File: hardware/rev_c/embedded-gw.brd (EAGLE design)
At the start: 38.5 x 66 mm, 57 parts, among them J1 DM3BT-DSF-PEJS, J2 TC2030-JLINK-NL, J3 USB-A-MALE-PLUG, Q1 QS5K2TR, U1 AP7362A-33SP-13, U2 BT840X, U3 CP2102N-20, U4 ESDR0502N, U5 ESP32-WROVER-E, U6 ESP32-WROVER-E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

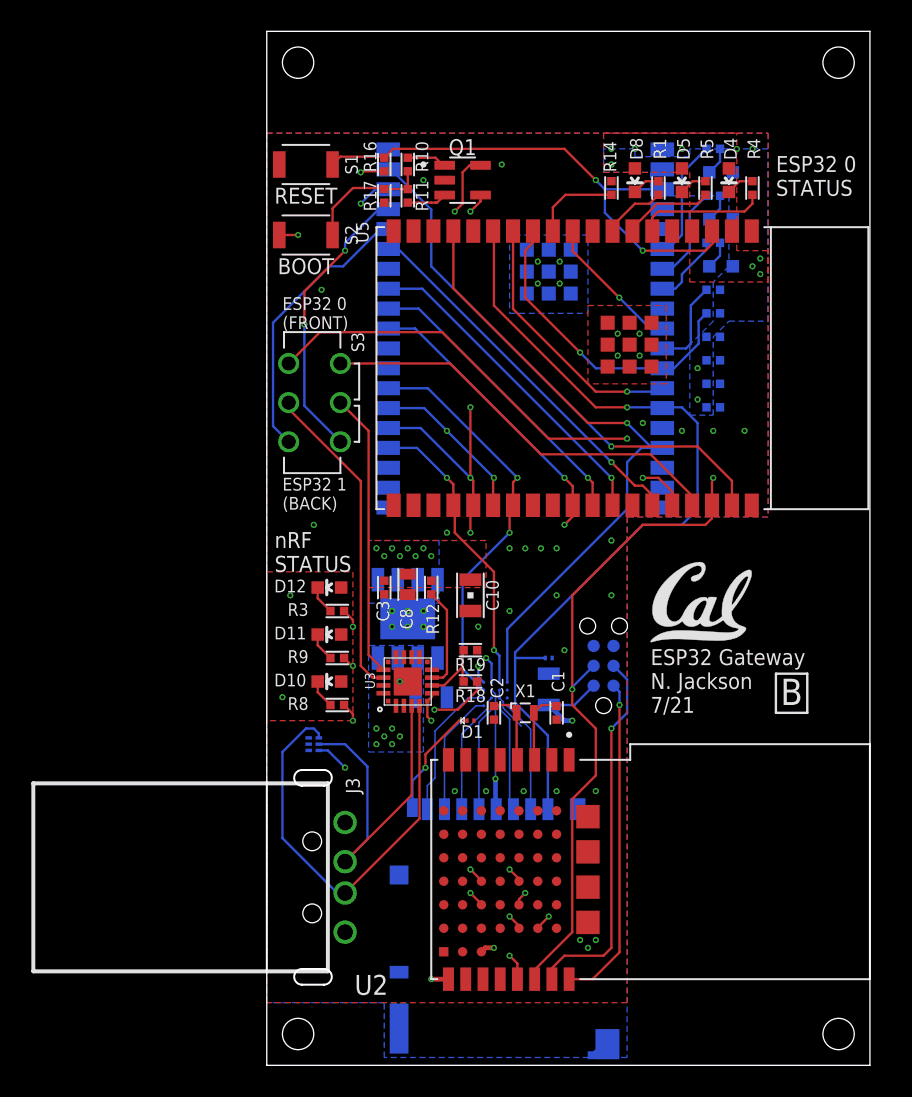
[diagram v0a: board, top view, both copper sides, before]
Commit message: replace sd card slot
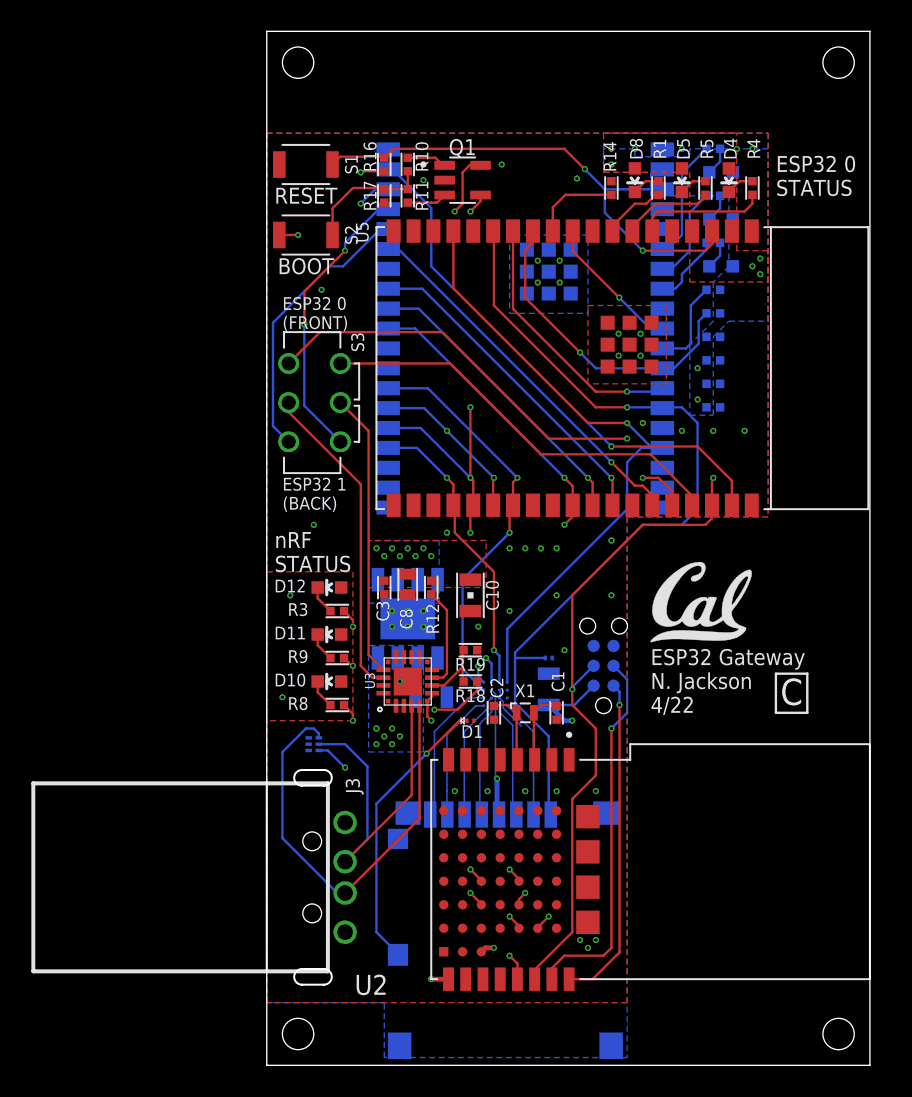
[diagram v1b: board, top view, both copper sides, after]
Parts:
- J1: value DM3BT-DSF-PEJS -> 5027740891; device connector:HRS_DM3BT-DSF-PEJS -> connector:5027740891
- moved J1 1.25 mm to (14.8, 12.8), turned to 180 degrees
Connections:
- net !SD_INSERTED: now also J1.SWITCH; no longer J1.SW-B
- net GND: now also J1.DETECT, J1.GND1, J1.GND2, J1.GND3, J1.GND4; no longer J1.S1, J1.S2, J1.S3, J1.S4, J1.SW-A
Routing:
- net !SD_INSERTED: track 59.2 -> 69.2 mm
- net VCC: track 21.6 -> 22.1 mm
- net GND: track 10.8 -> 11.1 mm, vias 44 -> 45
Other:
- board text added: "ESP32 Gateway N. Jackson 4/22"
- board text removed: "ESP32 Gateway N. Jackson 7/21"

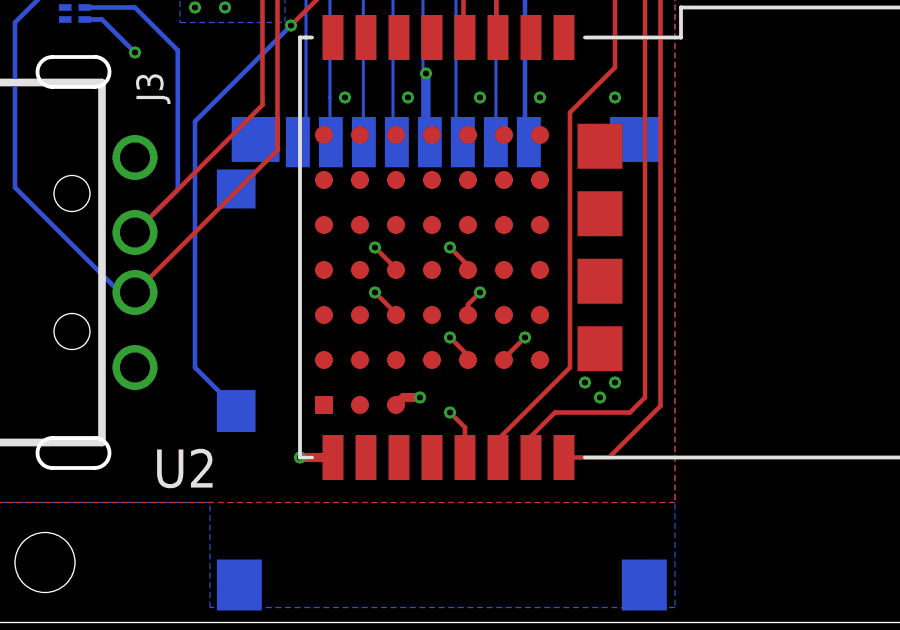
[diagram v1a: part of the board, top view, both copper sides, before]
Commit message: change sclk to pin 16 instead of PA 19
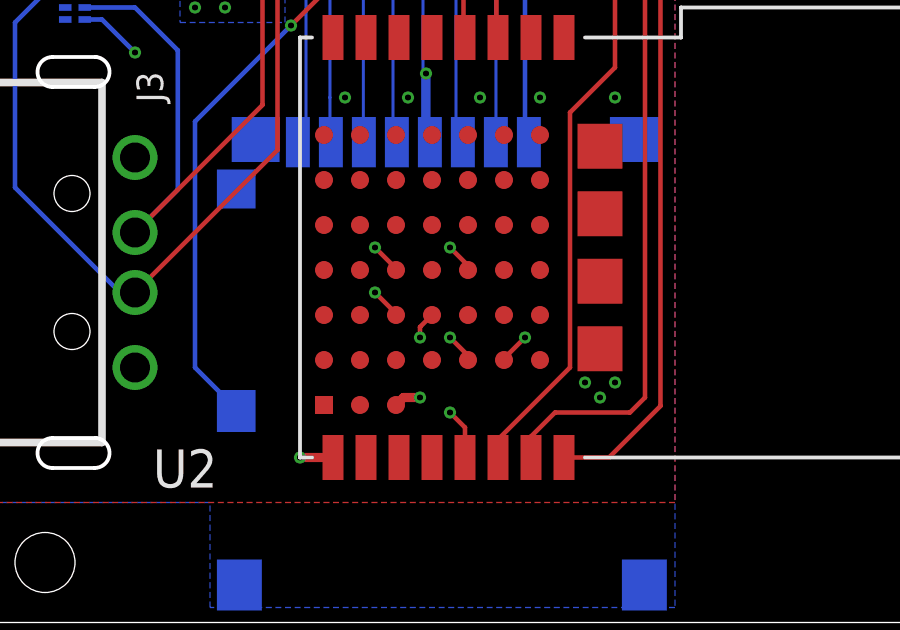
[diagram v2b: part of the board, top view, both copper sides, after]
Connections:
- net NRF_SCLK: now also U2.D3; no longer U2.D2
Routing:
- net NRF_SCLK: track 48.2 -> 53.1 mm
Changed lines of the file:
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@@
 <setting verticaltext="up"/>
 </settings>
-<grid distance="0.1" unitdist="mm" unit="mm" style="lines" multiple="1" display="yes" altdistance="0.01" altunitdist="mm" altunit="mm"/>
+<grid distance="0.5" unitdist="mm" unit="mm" style="lines" multiple="1" display="yes" altdistance="0.01" altunitdist="mm" altunit="mm"/>
 <layers>
 <layer number="1" name="Top" color="4" fill="1" visible="yes" active="yes"/>
@@
 <contactref element="U5" pad="30"/>
 <contactref element="U6" pad="30"/>
-<contactref element="U2" pad="D2"/>
-<via x="16.5" y="7" extent="1-16" drill="0.2032"/>
-<wire x1="16.5" y1="7" x2="16.1" y2="6.6" width="0.1524" layer="1"/>
-<wire x1="16.1" y1="6.6" x2="16.1" y2="6.25" width="0.1524" layer="1"/>
 <wire x1="7.75" y1="44.3" x2="9.7" y2="44.3" width="0.1524" layer="16"/>
 <via x="20.5" y="33.5" extent="1-16" drill="0.2032"/>
@@
 <wire x1="20.8" y1="33.2" x2="20.8" y2="31.75" width="0.1524" layer="1"/>
 <wire x1="9.7" y1="44.3" x2="20.5" y2="33.5" width="0.1524" layer="16"/>
-<wire x1="16.5" y1="7" x2="17" y2="7.5" width="0.1524" layer="2"/>
-<wire x1="17" y1="30" x2="17" y2="7.5" width="0.1524" layer="2"/>
-<wire x1="17" y1="30" x2="20.5" y2="33.5" width="0.1524" layer="2"/>
+<wire x1="20.5" y1="33.5" x2="17" y2="30" width="0.1524" layer="2"/>
+<contactref element="U2" pad="D3"/>
+<wire x1="17" y1="5.5" x2="16" y2="4.5" width="0.1524" layer="2"/>
+<wire x1="16" y1="4.5" x2="15" y2="4.5" width="0.1524" layer="2"/>
+<wire x1="15" y1="4.5" x2="14.5" y2="5" width="0.1524" layer="2"/>
+<wire x1="17" y1="30" x2="17" y2="5.5" width="0.1524" layer="2"/>
+<wire x1="14.5" y1="5" x2="14.5" y2="5.5" width="0.1524" layer="2"/>
+<via x="14.5" y="5.5" extent="1-16" drill="0.2032"/>
+<wire x1="14.5" y1="5.5" x2="14.5" y2="5.85" width="0.1524" layer="1"/>
+<wire x1="14.5" y1="5.85" x2="14.9" y2="6.25" width="0.1524" layer="1"/>
 </signal>
 <signal name="NRF_MISO">
